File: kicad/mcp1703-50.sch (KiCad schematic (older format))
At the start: 3 parts, among them U3 MCP1703A-3302_SOT23

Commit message: updates
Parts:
- removed C4, C5: 1uF, Capacitor_SMD:C_0805_2012Metric_Pad1.15x1.40mm_HandSolder, symbol Device:C
- removed U3: MCP1703A-3302_SOT23, Package_TO_SOT_SMD:SOT-23, symbol Regulator_Linear:MCP1703A-3302_SOT23
- added C6, C7: 1uF, Capacitor_SMD:C_0805_2012Metric_Pad1.15x1.40mm_HandSolder, symbol Device:C
- added U5: MCP1703A-5002_SOT23, Package_TO_SOT_SMD:SOT-23, symbol Regulator_Linear:MCP1703A-5002_SOT23
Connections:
- net 3.3V: now also C7.2, U5.2 (VO)
- net GND: now also C6.1, C7.1, U5.1 (GND)
- net VDD: now also C6.2, U5.3 (VI)
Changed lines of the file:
@@
 $Descr A4 11693 8268
 encoding utf-8
-Sheet 3 4
+Sheet 4 4
 Title ""
 Date ""
@@
 NoConn ~ 7250 2750
 $Comp
-L Device:C C5
-U 1 1 5C39965E
+L Device:C C7
+U 1 1 5C3D397C
 P 5900 4150
-F 0 "C5" H 5785 4104 50  0000 R CNN
+F 0 "C7" H 5785 4104 50  0000 R CNN
 F 1 "1uF" H 5785 4195 50  0000 R CNN
 F 2 "Capacitor_SMD:C_0805_2012Metric_Pad1.15x1.40mm_HandSolder" H 5938 4000 50  0001 C CNN
@@
 $EndComp
 $Comp
-L Device:C C4
-U 1 1 5C3997D6
+L Device:C C6
+U 1 1 5C3D397D
 P 4650 4150
-F 0 "C4" H 4535 4104 50  0000 R CNN
+F 0 "C6" H 4535 4104 50  0000 R CNN
 F 1 "1uF" H 4535 4195 50  0000 R CNN
 F 2 "Capacitor_SMD:C_0805_2012Metric_Pad1.15x1.40mm_HandSolder" H 4688 4000 50  0001 C CNN
@@
 	-1   0    0    1
 $EndComp
-$Comp
-L Regulator_Linear:MCP1703A-3302_SOT23 U3
-U 1 1 5C3998E1
-P 5300 4000
-F 0 "U3" H 5300 4242 50  0000 C CNN
-F 1 "MCP1703A-3302_SOT23" H 5300 4151 50  0000 C CNN
-F 2 "Package_TO_SOT_SMD:SOT-23" H 5300 4200 50  0001 C CNN
-F 3 "http://ww1.microchip.com/downloads/en/DeviceDoc/20005122B.pdf" H 5300 3950 50  0001 C CNN
-	1    5300 4000
-	1    0    0    -1
-$EndComp
 Wire Wire Line
 	4650 4000 5000 4000
@@
 	5600 4000 5900 4000
 $Comp
-L power:GND #PWR0109
-U 1 1 5C3999A1
+L power:GND #PWR0125
+U 1 1 5C3D397E
 P 5300 4400
-F 0 "#PWR0109" H 5300 4150 50  0001 C CNN
+F 0 "#PWR0125" H 5300 4150 50  0001 C CNN
 F 1 "GND" H 5305 4227 50  0000 C CNN
 F 2 "" H 5300 4400 50  0001 C CNN
@@
 $EndComp
 $Comp
-L power:GND #PWR0110
-U 1 1 5C399A71
+L power:GND #PWR0126
+U 1 1 5C3D397F
 P 5900 4400
-F 0 "#PWR0110" H 5900 4150 50  0001 C CNN
+F 0 "#PWR0126" H 5900 4150 50  0001 C CNN
 F 1 "GND" H 5905 4227 50  0000 C CNN
 F 2 "" H 5900 4400 50  0001 C CNN
@@
 $EndComp
 $Comp
-L power:GND #PWR0111
-U 1 1 5C399A88
+L power:GND #PWR0127
+U 1 1 5C3D3980
 P 4650 4400
-F 0 "#PWR0111" H 4650 4150 50  0001 C CNN
+F 0 "#PWR0127" H 4650 4150 50  0001 C CNN
 F 1 "GND" H 4655 4227 50  0000 C CNN
 F 2 "" H 4650 4400 50  0001 C CNN
@@
 Text HLabel 6650 4000 2    50   Output ~ 0
 3.3V
+$Comp
+L Regulator_Linear:MCP1703A-5002_SOT23 U5
+U 1 1 5C3D1B9E
+P 5300 4000
+F 0 "U5" H 5300 4242 50  0000 C CNN
+F 1 "MCP1703A-5002_SOT23" H 5300 4151 50  0000 C CNN
+F 2 "Package_TO_SOT_SMD:SOT-23" H 5300 4200 50  0001 C CNN
+F 3 "http://ww1.microchip.com/downloads/en/DeviceDoc/20005122B.pdf" H 5300 3950 50  0001 C CNN
+	1    5300 4000
+	1    0    0    -1
+$EndComp
 $EndSCHEMATC

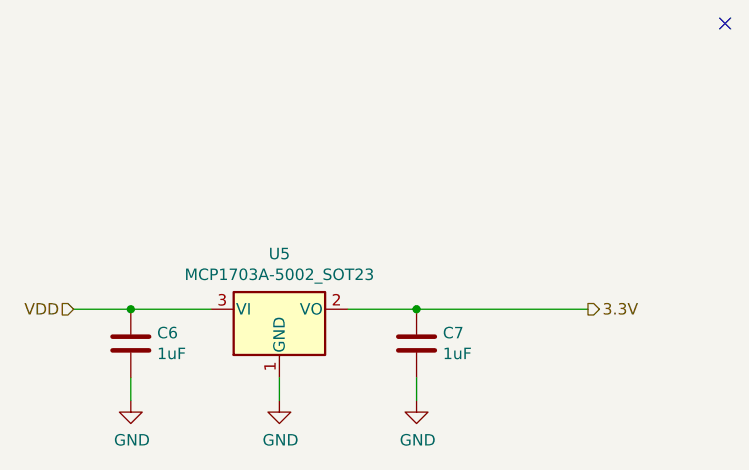
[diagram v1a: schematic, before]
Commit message: add test points in kicad
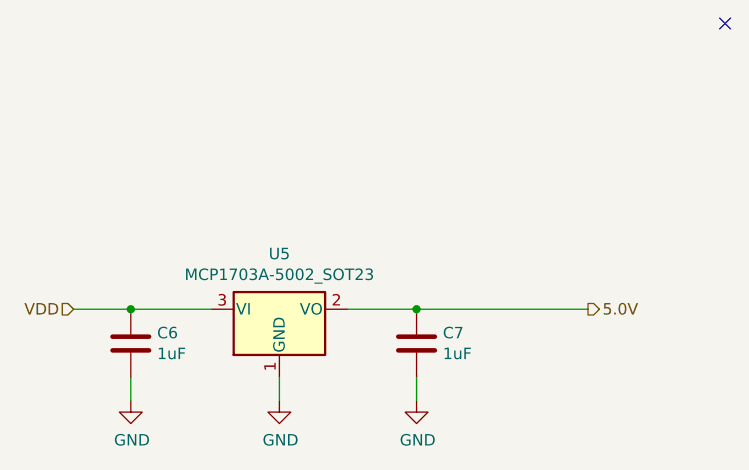
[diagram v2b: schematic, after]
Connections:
- net 3.3V renamed 5.0V
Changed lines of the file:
@@
 	4650 4000 4400 4000
 Connection ~ 4650 4000
-Wire Wire Line
-	5900 4000 6650 4000
 Text HLabel 4400 4000 0    50   Input ~ 0
 VDD
 Text HLabel 6650 4000 2    50   Output ~ 0
-3.3V
+5.0V
 $Comp
 L Regulator_Linear:MCP1703A-5002_SOT23 U5
@@
 	1    0    0    -1
 $EndComp
+Wire Wire Line
+	5900 4000 6650 4000
 $EndSCHEMATC

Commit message: add more test points
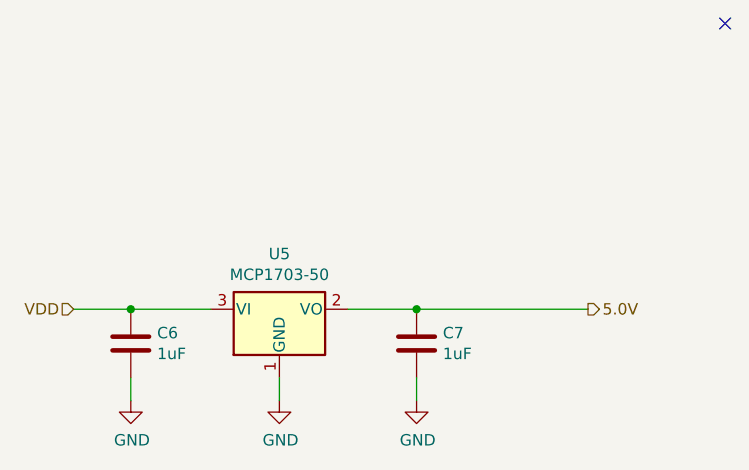
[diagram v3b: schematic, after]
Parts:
- U5: value MCP1703A-5002_SOT23 -> MCP1703-50
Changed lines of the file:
@@
 P 5300 4000
 F 0 "U5" H 5300 4242 50  0000 C CNN
-F 1 "MCP1703A-5002_SOT23" H 5300 4151 50  0000 C CNN
+F 1 "MCP1703-50" H 5300 4151 50  0000 C CNN
 F 2 "Package_TO_SOT_SMD:SOT-23" H 5300 4200 50  0001 C CNN
 F 3 "http://ww1.microchip.com/downloads/en/DeviceDoc/20005122B.pdf" H 5300 3950 50  0001 C CNN
